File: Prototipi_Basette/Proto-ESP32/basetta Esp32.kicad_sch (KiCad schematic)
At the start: 33 parts, among them J1 Conn_01x19, J2 Conn_01x19, J3 Conn_01x19, J4 Conn_01x19, J5 Screw_Terminal_01x02, J6 Conn_01x05, J7 Conn_01x02, J8 Conn_01x05, J9 Conn_01x05, Q1 BC547, Q2 BC547, Q4 BC547, Q5 BC557, Q6 IRF9540N, SW1 RESET, SW2 SET, U3 4013

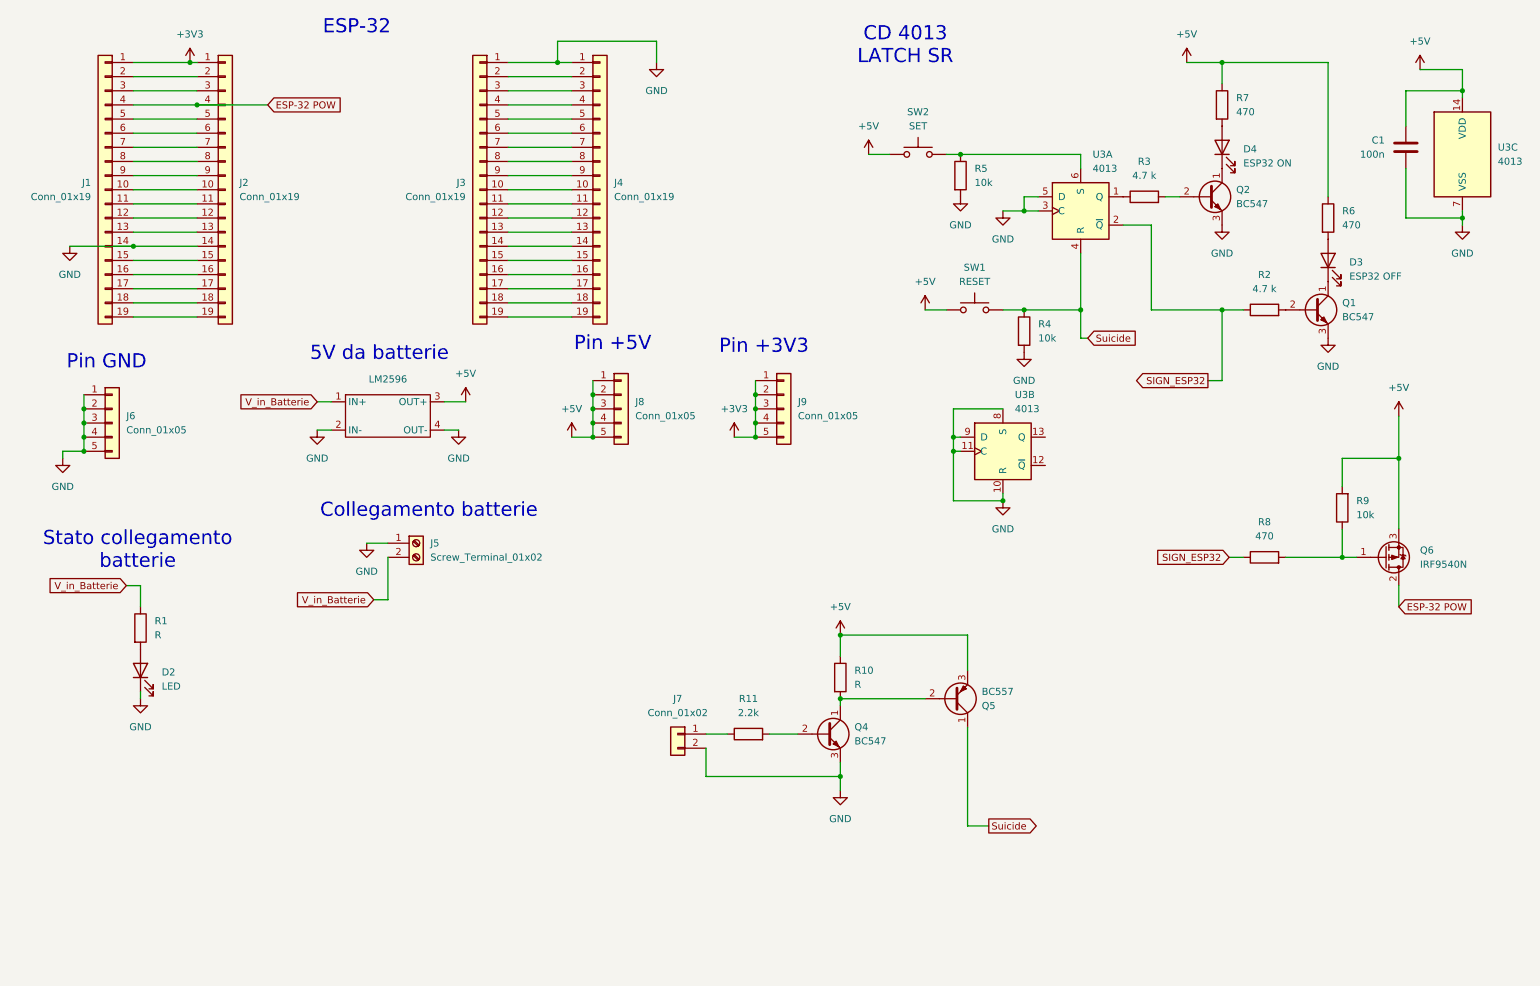
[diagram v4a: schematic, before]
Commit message: Add mounting holes and tidy PCB footprints
Added two M3 mounting-hole footprints and multiple thru-hole pads (GND connected). Cleaned up many footprints by hiding F.Fab value/reference texts, removing redundant fp_text user elements, and adjusting reference designators (several Q/R/J renames). Updated component positions (connectors/terminal block), fixed net assignments for several pads/nets, and refreshed UUIDs across footprints. Overall PCB housekeeping and footprint consistency updates.
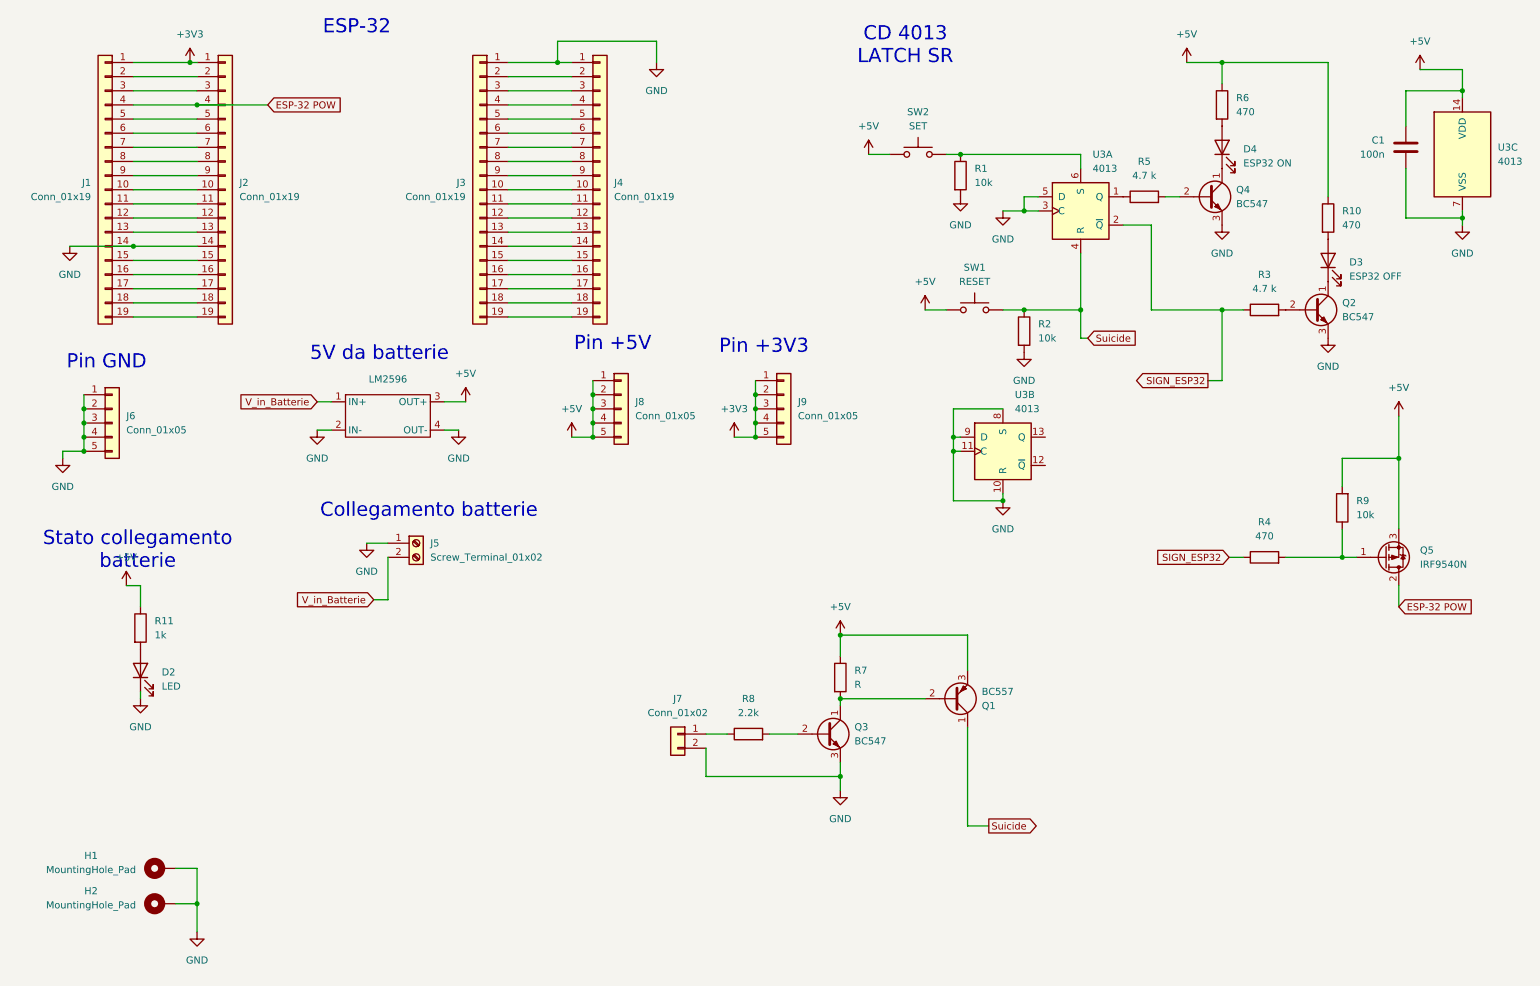
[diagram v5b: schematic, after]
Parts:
- added H1, H2: MountingHole_Pad, MountingHole:MountingHole_3.2mm_M3_Pad_Via, symbol Mechanical:MountingHole_Pad
- R11: renamed from R1; value R -> 1k
- renumbered Q5 to Q1, Q1 to Q2, Q4 to Q3, Q2 to Q4, Q6 to Q5, R5 to R1, R6 to R10, R4 to R2, R2 to R3, R8 to R4, R3 to R5, R7 to R6, R10 to R7, R11 to R8
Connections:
- net +5V: now also R11.1
- net GND: now also H1.1, H2.1
- net V_in_Batterie: no longer R11.1

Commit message: Update ESP32 prototype files and add Gerbers
Remove obsolete Basetta_ESP32.zip and ITTCV-TDP-04 KiCad variant files; apply updates to the main KiCad project files (basetta Esp32.kicad_pcb, .kicad_prl, .kicad_pro, .kicad_sch). Add Gerber.zip with manufacturing outputs. Cleans up old artifacts and includes updated PCB/project metadata for the ESP32 prototype.
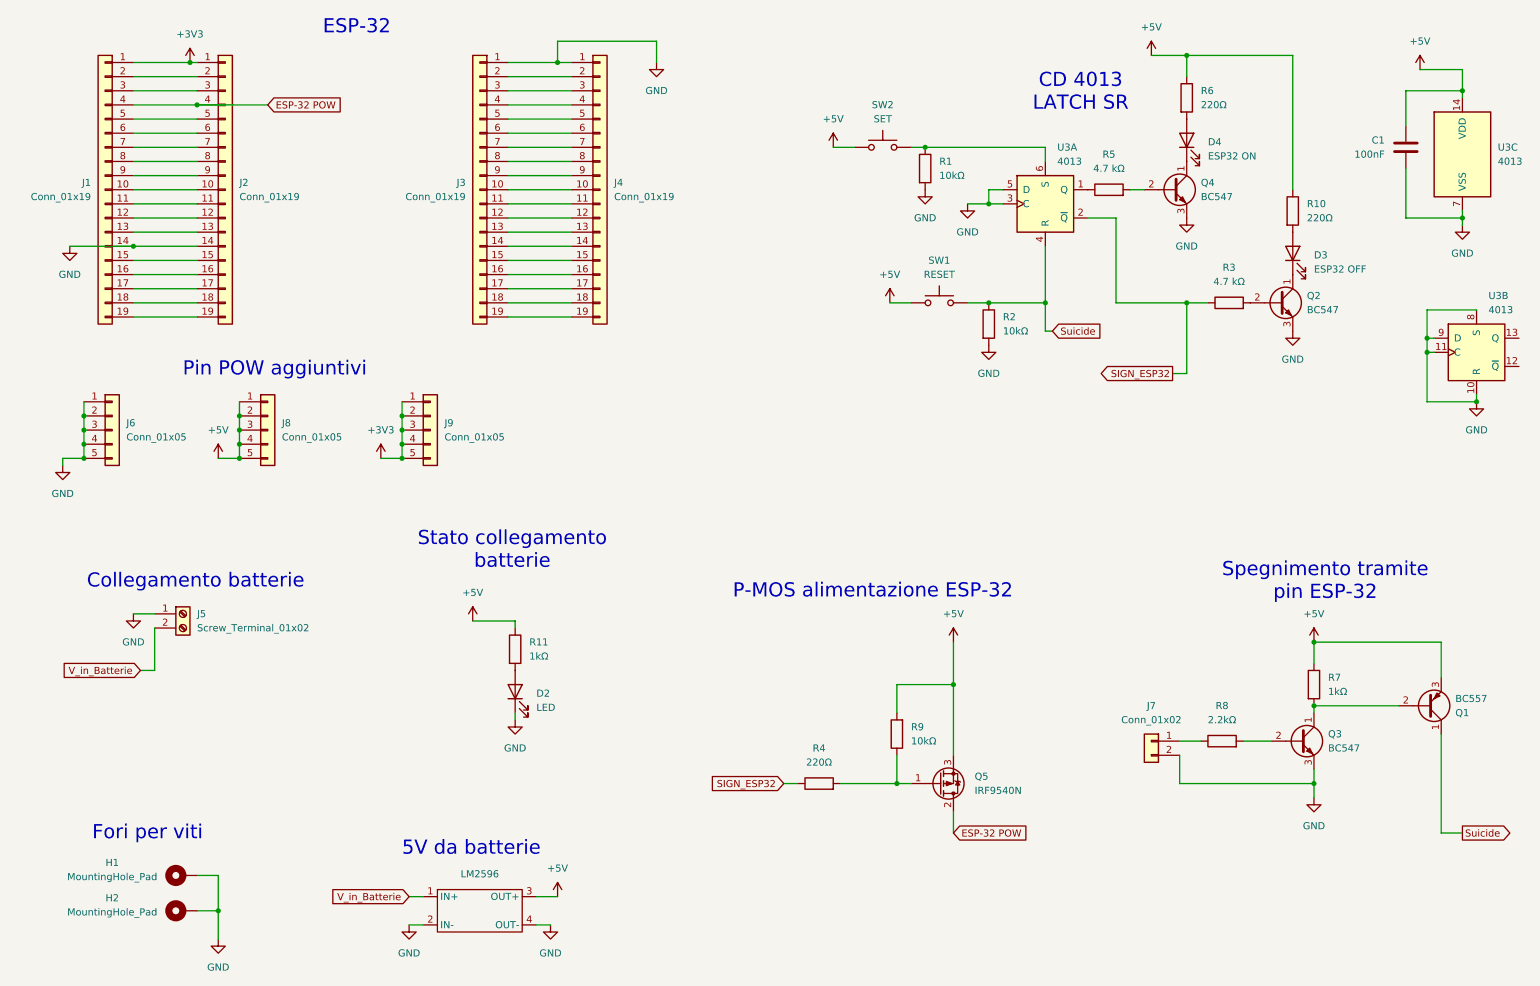
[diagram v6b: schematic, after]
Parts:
- C1: value 100n -> 100nF
- R1, R2, R9: value 10k -> 10kΩ
- R10, R4, R6: value 470 -> 220Ω
- R11: value 1k -> 1kΩ
- R3, R5: value 4.7 k -> 4.7 kΩ
- R7: value R -> 1kΩ
- R8: value 2.2k -> 2.2kΩ
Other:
- note added: "Fori per viti"
- note added: "P-MOS alimentazione ESP-32"
- note added: "Pin POW aggiuntivi"
- note added: "Spegnimento tramite pin ESP-32"
- note removed: "Pin +3V3"
- note removed: "Pin +5V"
- note removed: "Pin GND"
- moved on the sheet: D2, D3, D4, H1, H2, J5, J6, J7, J8, J9, LM2596, Q1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
